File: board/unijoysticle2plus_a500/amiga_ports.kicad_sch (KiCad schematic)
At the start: 17 parts

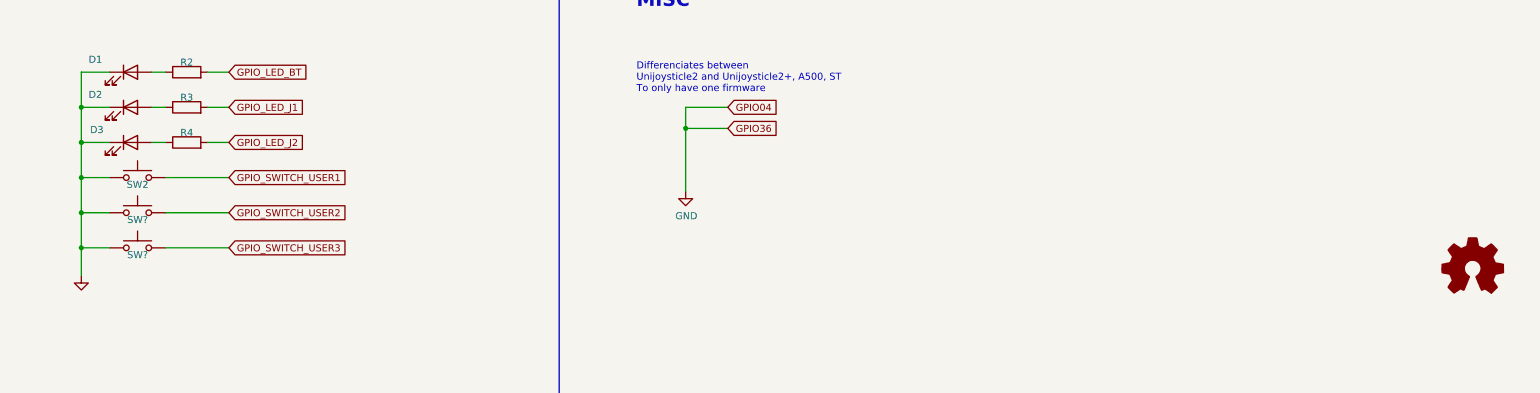
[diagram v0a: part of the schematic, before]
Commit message: a500: remove duplicate symbols
It is able to run the EDR checks with 5 warnings.
Only one looks worth taking a look at.
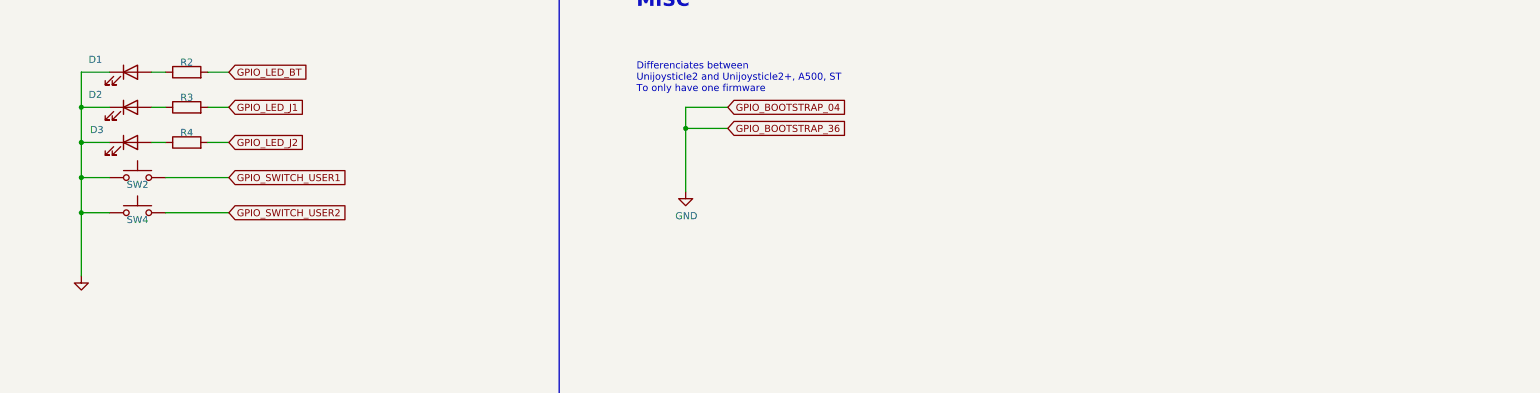
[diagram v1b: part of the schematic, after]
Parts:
- removed SW?: ~, symbol Switch:SW_Push
- U3: value (none) -> ~
- gave numbers to parts that had none: 1
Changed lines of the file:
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@@
   (junction (at 133.35 148.59) (diameter 0) (color 0 0 0 0)
   )
-  (junction (at 24.13 170.18) (diameter 0) (color 0 0 0 0)
-  )
   (wire (pts (xy 36.83 45.72) (xy 24.13 45.72))
     (stroke (width 0) (type default) (color 0 0 0 0))
@@
     (stroke (width 0) (type default) (color 0 0 0 0))
   )
-  (wire (pts (xy 24.13 163.83) (xy 24.13 170.18))
-    (stroke (width 0) (type default) (color 0 0 0 0))
-  )
   (polyline (pts (xy 285.75 116.84) (xy 285.75 118.11))
     (stroke (width 0) (type default) (color 0 0 0 0))
@@
     (stroke (width 0) (type default) (color 0 0 0 0))
   )
-  (wire (pts (xy 24.13 170.18) (xy 29.21 170.18))
-    (stroke (width 0) (type default) (color 0 0 0 0))
-  )
   (wire (pts (xy 260.35 48.26) (xy 267.97 48.26))
     (stroke (width 0) (type default) (color 0 0 0 0))
@@
     (stroke (width 0) (type default) (color 0 0 0 0))
   )
-  (wire (pts (xy 39.37 170.18) (xy 50.8 170.18))
-    (stroke (width 0) (type default) (color 0 0 0 0))
-  )
   (wire (pts (xy 156.21 50.8) (xy 166.37 50.8))
     (stroke (width 0) (type default) (color 0 0 0 0))
@@
     (stroke (width 0) (type default) (color 0 0 0 0))
   )
-  (wire (pts (xy 24.13 170.18) (xy 24.13 175.26))
+  (wire (pts (xy 24.13 163.83) (xy 24.13 175.26))
     (stroke (width 0) (type default) (color 0 0 0 0))
   )
@@
     )
   )
-  (global_label "GPIO36" (shape input) (at 140.97 148.59 0) (fields_autoplaced)
+  (global_label "GPIO_BOOTSTRAP_36" (shape input) (at 140.97 148.59 0) (fields_autoplaced)
     (effects (font (size 1.27 1.27)) (justify left))
-    (property "Intersheet References" "${INTERSHEET_REFS}" (id 0) (at 150.1885 148.5106 0)
+    (property "Intersheet References" "${INTERSHEET_REFS}" (id 0) (at 162.828 148.5106 0)
       (effects (font (size 1.27 1.27)) (justify left) hide)
     )
@@
     )
   )
-  (global_label "GPIO04" (shape input) (at 140.97 144.78 0) (fields_autoplaced)
+  (global_label "GPIO_BOOTSTRAP_04" (shape input) (at 140.97 144.78 0) (fields_autoplaced)
     (effects (font (size 1.27 1.27)) (justify left))
-    (property "Intersheet References" "${INTERSHEET_REFS}" (id 0) (at 150.1885 144.7006 0)
+    (property "Intersheet References" "${INTERSHEET_REFS}" (id 0) (at 162.828 144.7006 0)
       (effects (font (size 1.27 1.27)) (justify left) hide)
     )
@@
     )
   )
-  (global_label "GPIO_SWITCH_USER3" (shape input) (at 50.8 170.18 0) (fields_autoplaced)
-    (effects (font (size 1.27 1.27)) (justify left))
-    (property "Intersheet References" "${INTERSHEET_REFS}" (id 0) (at 72.5371 170.1006 0)
-      (effects (font (size 1.27 1.27)) (justify left) hide)
-    )
-  )
   (global_label "GPIO_J1_RIGHT" (shape input) (at 139.7 60.96 180) (fields_autoplaced)
     (effects (font (size 1.27 1.27)) (justify right))
@@
     (in_bom yes) (on_board yes)
     (property "Reference" "U3" (id 0) (at 252.73 54.61 0))
-    (property "Value" "" (id 1) (at 252.73 52.6796 0))
+    (property "Value" "~" (id 1) (at 252.73 52.6796 0))
     (property "Footprint" "" (id 2) (at 252.73 58.42 0)
       (effects (font (size 1.27 1.27)) hide)
@@
     (in_bom yes) (on_board yes)
     (property "Reference" "U3" (id 0) (at 252.73 66.04 0))
-    (property "Value" "" (id 1) (at 252.73 64.1096 0))
+    (property "Value" "~" (id 1) (at 252.73 64.1096 0))
     (property "Footprint" "" (id 2) (at 252.73 69.85 0)
       (effects (font (size 1.27 1.27)) hide)
@@
     (pin "1")
   )
-  (symbol (lib_id "Graphic:Logo_Open_Hardware_Small") (at 275.59 173.99 0) (unit 1)
-    (in_bom yes) (on_board yes)
-    (property "Reference" "#LOGO1" (id 0) (at 275.59 166.5224 0)
-      (effects (font (size 1.27 1.27)) hide)
-    )
-    (property "Value" "~" (id 1) (at 275.59 179.705 0)
-      (effects (font (size 1.27 1.27)) hide)
-    )
-    (property "Footprint" "" (id 2) (at 275.59 173.99 0)
-      (effects (font (size 1.27 1.27)) hide)
-    )
-    (property "Datasheet" "~" (id 3) (at 275.59 173.99 0)
-      (effects (font (size 1.27 1.27)) hide)
-    )
-  )
   (symbol (lib_id "Device:LED") (at 33.02 138.43 0) (unit 1)
     (in_bom yes) (on_board yes)
@@
     (in_bom yes) (on_board yes)
     (property "Reference" "U3" (id 0) (at 252.73 31.75 0))
-    (property "Value" "" (id 1) (at 252.73 31.0896 0))
+    (property "Value" "~" (id 1) (at 252.73 31.0896 0))
     (property "Footprint" "" (id 2) (at 252.73 36.83 0)
       (effects (font (size 1.27 1.27)) hide)
@@
     (in_bom yes) (on_board yes)
     (property "Reference" "U3" (id 0) (at 252.73 44.45 0))
-    (property "Value" "" (id 1) (at 260.35 39.9796 0))
+    (property "Value" "~" (id 1) (at 260.35 39.9796 0))
     (property "Footprint" "" (id 2) (at 252.73 48.26 0)
       (effects (font (size 1.27 1.27)) hide)
@@
     (in_bom yes) (on_board yes)
     (property "Reference" "U3" (id 0) (at 252.73 80.8482 90))
-    (property "Value" "" (id 1) (at 252.73 83.1596 90))
+    (property "Value" "~" (id 1) (at 252.73 83.1596 90))
     (property "Footprint" "" (id 2) (at 252.73 90.17 0)
       (effects (font (size 1.27 1.27)) hide)
@@
     (pin "1")
   )
-  (symbol (lib_id "Switch:SW_Push") (at 34.29 170.18 0) (unit 1)
-    (in_bom yes) (on_board yes)
-    (property "Reference" "SW?" (id 0) (at 34.29 171.45 0))
-    (property "Value" "~" (id 1) (at 34.29 173.99 0))
-    (property "Footprint" "" (id 2) (at 34.29 165.1 0)
-      (effects (font (size 1.27 1.27)) hide)
-    )
-    (property "Datasheet" "~" (id 3) (at 34.29 165.1 0)
-      (effects (font (size 1.27 1.27)) hide)
-    )
-    (pin "1")
-    (pin "2")
-  )
   (symbol (lib_id "Switch:SW_Push") (at 34.29 163.83 0) (unit 1)
     (in_bom yes) (on_board yes)
-    (property "Reference" "SW?" (id 0) (at 34.29 165.1 0))
+    (property "Reference" "SW4" (id 0) (at 34.29 165.1 0))
     (property "Value" "~" (id 1) (at 34.29 167.64 0))
     (property "Footprint" "" (id 2) (at 34.29 158.75 0)
@@
   (symbol (lib_id "power:GND") (at 133.35 160.02 0) (unit 1)
     (in_bom yes) (on_board yes)
-    (property "Reference" "#PWR?" (id 0) (at 133.35 166.37 0)
+    (property "Reference" "#PWR06" (id 0) (at 133.35 166.37 0)
       (effects (font (size 1.27 1.27)) hide)
     )
@@
       (reference "#FLG0102") (unit 1) (value "PWR_FLAG") (footprint "")
     )
-    (path "/00000000-0000-0000-0000-000060c7eeff"
-      (reference "#LOGO1") (unit 1) (value "Logo_Open_Hardware_Small") (footprint "")
-    )
     (path "/00000000-0000-0000-0000-000060c63ad6"

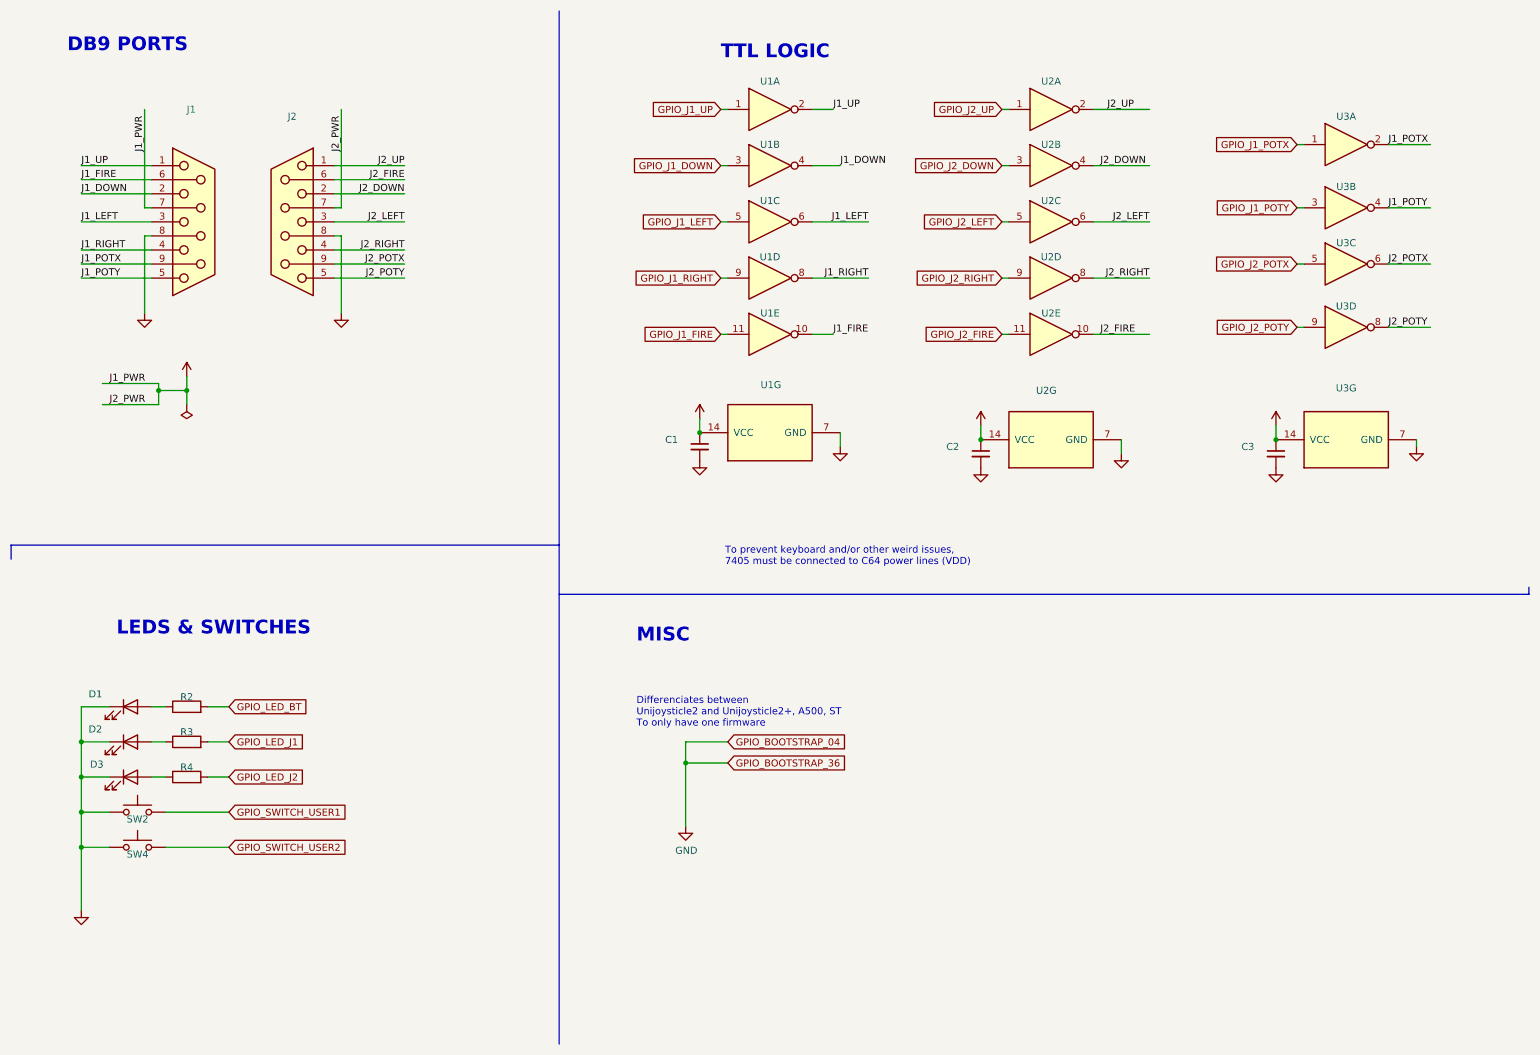
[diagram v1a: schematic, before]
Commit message: uni2+ a500: schematic "ready"
The schematic should be "ready".
Layout WIP. Components were placed in "place".
But routing is missing, as well as logos
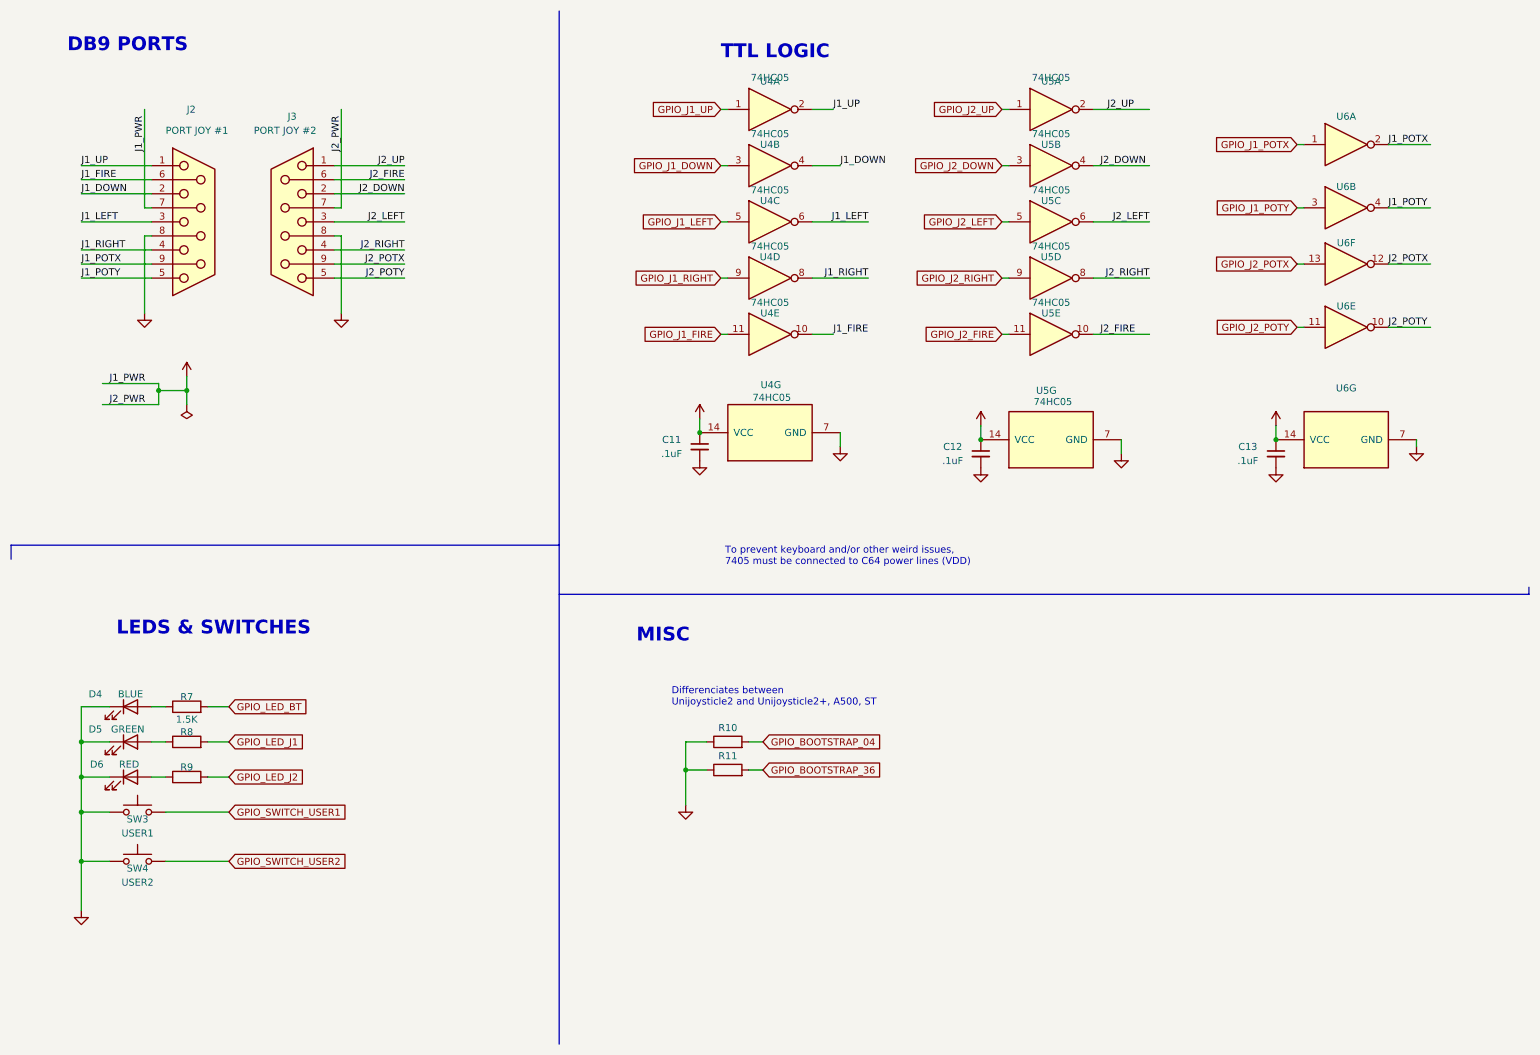
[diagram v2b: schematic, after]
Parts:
- added R10, R11: (no value), symbol Device:R
- C11: renamed from C1; value ~ -> .1uF; footprint (none) -> Capacitor_SMD:C_0805_2012Metric_Pad1.18x1.45mm_HandSolder
- C12: renamed from C2; value ~ -> .1uF; footprint (none) -> Capacitor_SMD:C_0805_2012Metric_Pad1.18x1.45mm_HandSolder
- C13: renamed from C3; value ~ -> .1uF; footprint (none) -> Capacitor_SMD:C_0805_2012Metric_Pad1.18x1.45mm_HandSolder
- D4: renamed from D1; value ~ -> BLUE; footprint (none) -> LED_SMD:LED_0805_2012Metric_Pad1.15x1.40mm_HandSolder
- D5: renamed from D2; value ~ -> GREEN; footprint (none) -> LED_SMD:LED_0805_2012Metric_Pad1.15x1.40mm_HandSolder
- D6: renamed from D3; value ~ -> RED; footprint (none) -> LED_SMD:LED_0805_2012Metric_Pad1.15x1.40mm_HandSolder
- J2: renamed from J1; value ~ -> PORT JOY #1; footprint (none) -> Connector_Dsub:DSUB-9_Female_Horizontal_P2.77x2.54mm_EdgePinOffset9.40mm
- J3: renamed from J2; value ~ -> PORT JOY #2; footprint (none) -> Connector_Dsub:DSUB-9_Female_Horizontal_P2.77x2.54mm_EdgePinOffset9.40mm
- R7: renamed from R2; value ~ -> 1.5K; footprint (none) -> Resistor_SMD:R_0805_2012Metric_Pad1.20x1.40mm_HandSolder
- R8: renamed from R3; value ~ -> (none)
- R9: renamed from R4; value ~ -> (none)
- SW3: renamed from SW2; value ~ -> USER1; footprint (none) -> Button_Switch_THT:SW_Tactile_SPST_Angled_PTS645Vx39-2LFS
- SW4: value ~ -> USER2; footprint (none) -> Button_Switch_THT:SW_Tactile_SPST_Angled_PTS645Vx39-2LFS
- U4: renamed from U1; value ~ -> 74HC05; footprint (none) -> Package_SO:SOIC-14_3.9x8.7mm_P1.27mm; LCSC (none) -> C7640
- U4: renamed from U1; value ~ -> 74HC05; footprint (none) -> Package_SO:SOIC-14_3.9x8.7mm_P1.27mm
- U5: renamed from U2; value ~ -> 74HC05; footprint (none) -> Package_SO:SOIC-14_3.9x8.7mm_P1.27mm; LCSC (none) -> C7640
- U5: renamed from U2; value ~ -> 74HC05; footprint (none) -> Package_SO:SOIC-14_3.9x8.7mm_P1.27mm
- U6: renamed from U3; value ~ -> (none)
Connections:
- net GND: now also R10.1, R11.1
- net GPIO_J2_POTX: now also U6.13; no longer U6.5
- net GPIO_J2_POTY: now also U6.11; no longer U6.9
- net J2_POTX: now also U6.12; no longer U6.6
- net J2_POTY: now also U6.10; no longer U6.8
- new net GPIO_BOOTSTRAP_04: R10.2
- new net GPIO_BOOTSTRAP_36: R11.2
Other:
- note added: "Differenciates between Unijoysticle2 and Unijoysticle2+, A500, ST"
- note removed: "Differenciates between Unijoysticle2 and Unijoysticle2+, A500, ST To only have one firmware"
- title: Unijoysticle 2+ -> Unijoysticle 2+ A500
- moved on the sheet: SW4

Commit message: uni a500: manual routing
WIP... all wires connected. requires to double check everything
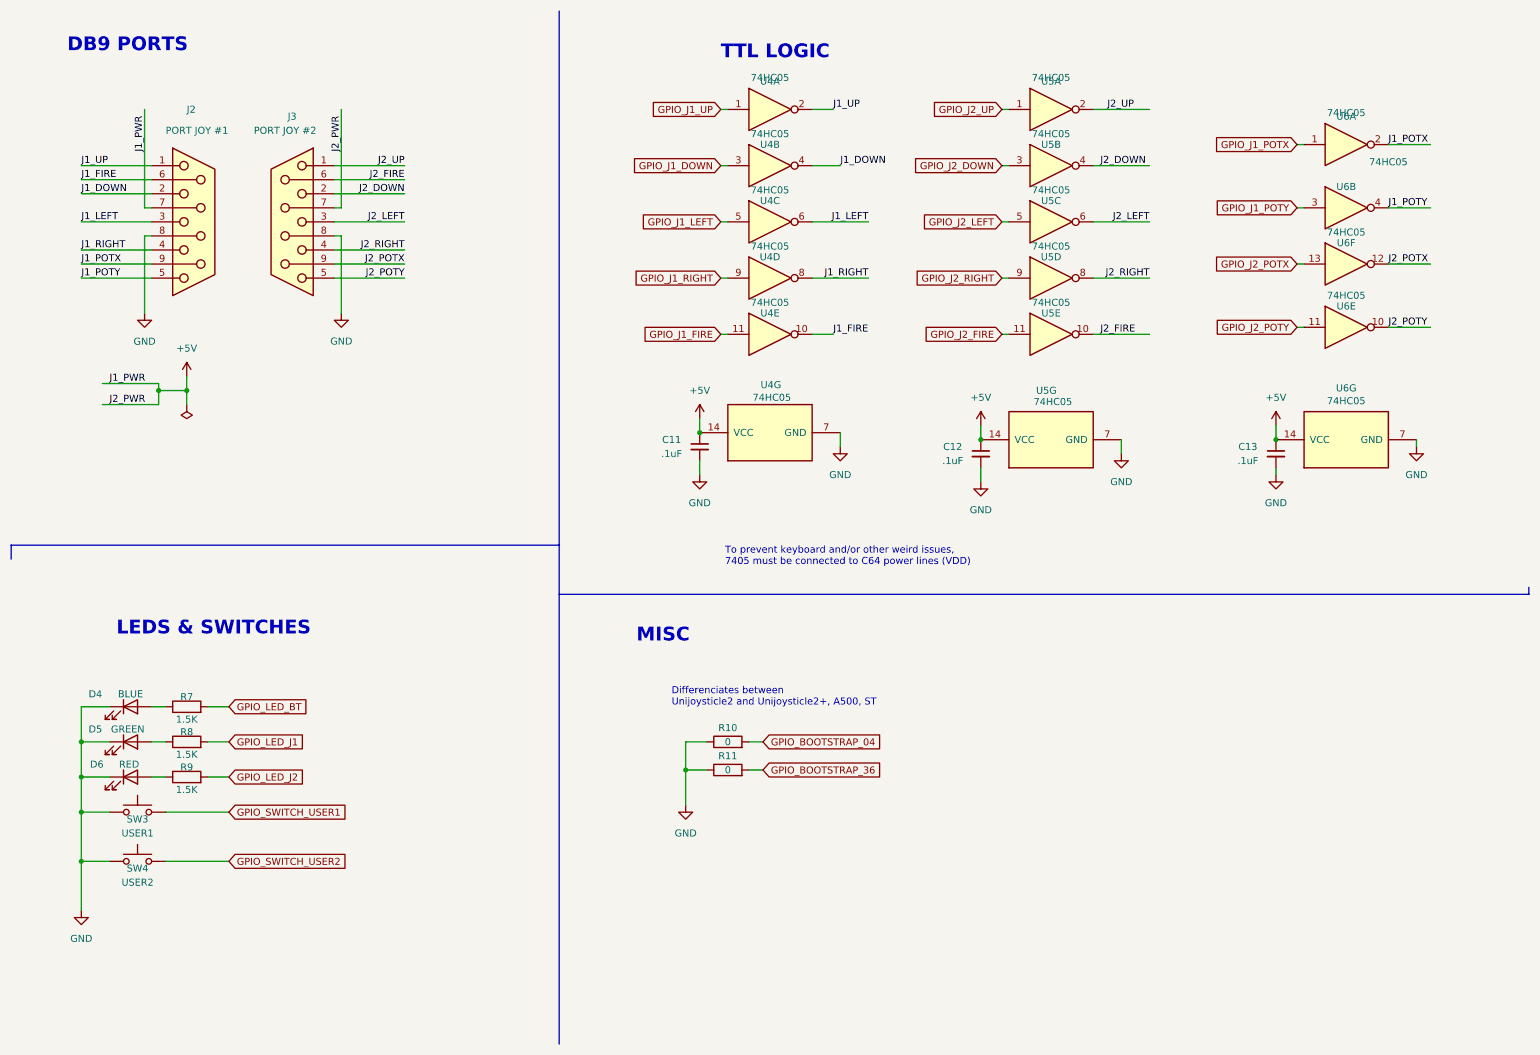
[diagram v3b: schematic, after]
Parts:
- R10, R11: value (none) -> 0; footprint (none) -> Resistor_SMD:R_0805_2012Metric_Pad1.20x1.40mm_HandSolder
- R8, R9: value (none) -> 1.5K; footprint (none) -> Resistor_SMD:R_0805_2012Metric_Pad1.20x1.40mm_HandSolder
- U6: value (none) -> 74HC05; footprint (none) -> Package_SO:SOIC-14_3.9x8.7mm_P1.27mm
